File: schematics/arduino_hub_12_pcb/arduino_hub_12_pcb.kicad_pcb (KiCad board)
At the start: 2 copper layers, 46 x 50.5 mm, 6 parts, among them J3 Screw_Terminal_01x02, J4 Conn_02x08_Odd_Even, U1 SN75176AP

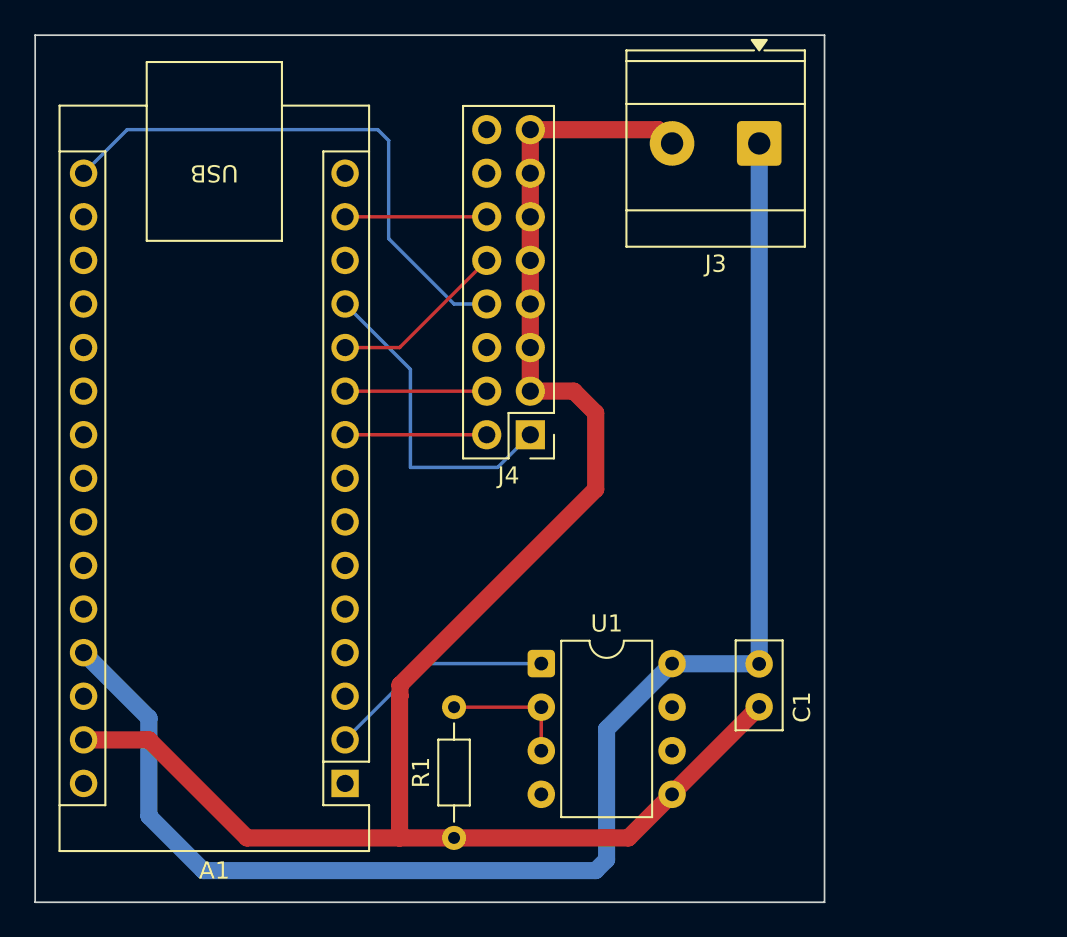
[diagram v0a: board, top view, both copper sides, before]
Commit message: added xlr connector
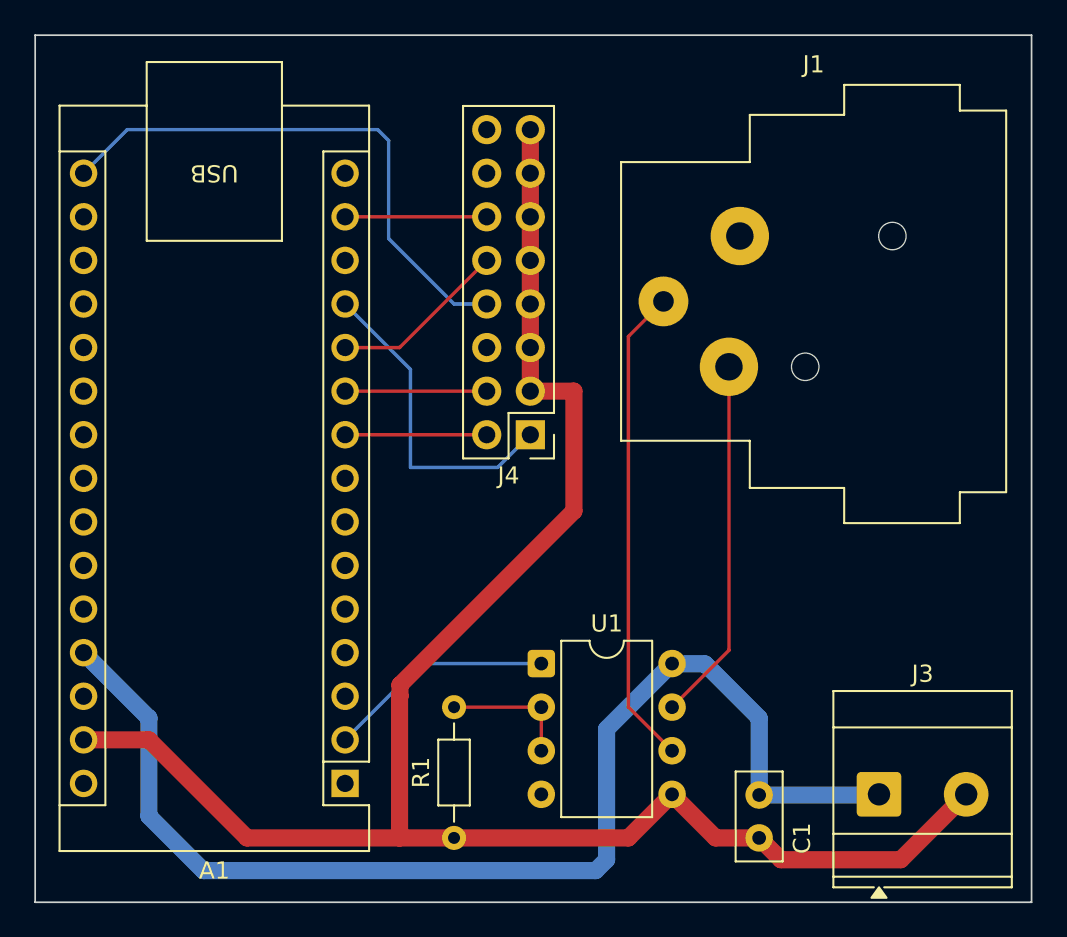
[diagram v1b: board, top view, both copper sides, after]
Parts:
- added J1: XLR3, Connector_Audio:Jack_XLR_Neutrik_NC3FAH-0_Horizontal, F.Cu at (55.4, 26.5)
- moved J3 38.6 mm to (63.5, 59.1), turned to 0 degrees
- moved C1 7.64 mm to (56.5, 59.1)
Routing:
- net DATA+: track 0.00 -> 28.1 mm
- net DATA-: track 0.00 -> 21.2 mm
- net 5V: track 87.1 -> 70.2 mm
- net GND: track 102.6 -> 106.0 mm
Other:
- board size 46 x 50.5 mm -> 58.1 x 50.5 mm
